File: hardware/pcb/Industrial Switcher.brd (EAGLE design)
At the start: 100 x 100 mm, 45 parts, among them IC1 MSP430FR5739, IC2 HY-TFT220, Q1 IRFR5305, Q2 32 kHz, Q3 IRFZ34NS, Q4 IRFZ34NS, Q5 IRFZ34NS, Q6 IRFZ34NS, U1 TDA3664, U2 TPS76933, U3 LT1161CSWPBF

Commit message: Routing almost finished.
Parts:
- added C14: 68uF, rcl:PANASONIC_F
- added H1, H2, H3, H4: (no value), holes:3,0
- added POWER: (no value), SparkFun:SCREWTERMINAL-5MM-2
- C13: device rcl:C0603 -> rcl:C0805
- C6: value 100uF -> 68uF; device rcl:PANASONIC_G -> rcl:PANASONIC_F
- moved C13 255.4 mm to (15.7, 4.32), flipped to the bottom, turned to 180 degrees
- moved JP1 237.5 mm to (29.5, 3.30)
- moved IC2 234.8 mm to (13.0, 1.78), turned to 270 degrees
- moved LOAD1 221.3 mm to (84.8, 41.1), turned to 90 degrees
- moved Q2 220.2 mm to (20.6, 23.4)
- moved C3 217.6 mm to (23.1, 23.4), turned to 90 degrees
- moved C2 211.6 mm to (18.0, 23.4), turned to 90 degrees
- moved C6 204.2 mm to (40.6, 36.8), flipped to the bottom, turned to 270 degrees
- moved Q3 197.7 mm to (71.9, 38.1), flipped to the bottom
- moved LOAD2 188.7 mm to (84.8, 28.7), turned to 90 degrees
- moved R8 183.8 mm to (42.4, 28.1), flipped to the bottom, turned to 180 degrees
- moved Q4 166.3 mm to (56.9, 38.1), flipped to the bottom
- moved LOAD3 159.6 mm to (84.8, 16.3), turned to 90 degrees
- moved R9 156.0 mm to (42.4, 25.5), flipped to the bottom, turned to 180 degrees
- moved LOAD4 133.8 mm to (84.8, 3.81), turned to 90 degrees
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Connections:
- removed net N$1: D1.C, Q1.3, U1.1
- removed net N$16: R9.1, U3.17
- removed net N$17: R8.1, U3.19
- new net N$23: Q5.1, U3.16
- new net N$24: Q4.1, U3.14
- new net N$25: Q3.1, U3.12
- net +24V: now also C14.+, D1.C, Q1.3, U1.1; no longer Q1.4
- net GND: now also C14.-, POWER.2
- net N$10: now also R11.1, U3.19; no longer Q4.1, U3.16
- net N$13: now also POWER.1, Q1.4; no longer Q3.1, U3.18
- net N$18: now also Q6.1, U3.18; no longer R10.1, U3.15
- net N$4: now also R8.1; no longer R11.1
- net N$5: now also R9.1, U3.15; no longer Q6.1, U3.12
- net N$7: now also R10.1, U3.17; no longer Q5.1, U3.14
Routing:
- net +24V: track 0.00 -> 287.7 mm, vias 0 -> 6
- net N$25: track 0.00 -> 39.9 mm
- net N$18: track 0.00 -> 37.0 mm
- net N$13: track 0.00 -> 29.7 mm
- net N$24: track 0.00 -> 23.5 mm
- net N$23: track 0.00 -> 18.5 mm
- net +5V: track 0.00 -> 13.0 mm
- net N$2: track 0.00 -> 3.21 mm
- net N$7: track 0.00 -> 2.37 mm
- net N$5: track 0.00 -> 2.37 mm
- net N$4: track 0.00 -> 2.37 mm
- net N$10: track 0.00 -> 2.37 mm
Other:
- board size 100 x 100 mm -> 90 x 50 mm

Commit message: Rearranged pins for better layout.
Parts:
- moved H1 320.0 mm to (78.2, 43.8)
- moved H2 293.9 mm to (79.0, 6.48)
- moved C12 250.0 mm to (27.9, 20.8), turned to 90 degrees
- moved C10 235.7 mm to (25.1, 20.1), flipped to the bottom, turned to 180 degrees
- moved R12 234.8 mm to (25.4, 10.7)
- moved C9 232.9 mm to (25.7, 21.8), flipped to the bottom, turned to 180 degrees
- moved C11 230.3 mm to (25.4, 9.53)
- moved C8 224.9 mm to (19.3, 20.1), flipped to the bottom, turned to 180 degrees
- moved C7 222.0 mm to (19.3, 21.8), flipped to the bottom, turned to 180 degrees
- moved R2 207.9 mm to (31.0, 20.4)
- moved R3 205.8 mm to (31.0, 23.0)
- moved R4 203.6 mm to (31.0, 25.5)
- moved R5 201.4 mm to (31.0, 28.1)
- moved JP1 3.59 mm to (26.2, 1.91)
- moved R10 2.79 mm to (45.2, 23.0)
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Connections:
- net CS: now also IC1.2; no longer IC1.17
- net DB0: now also IC1.12; no longer IC1.9
- net DB1: now also IC1.11; no longer IC1.10
- net DB2: now also IC1.8; no longer IC1.11
- net DB3: now also IC1.7; no longer IC1.12
- net DB4: now also IC1.6; no longer IC1.13
- net DB5: now also IC1.5; no longer IC1.14
- net DB6: now also IC1.4; no longer IC1.15
- net DB7: now also IC1.3; no longer IC1.16
- net DCLK: now also IC1.27; no longer IC1.29
- net DCS: now also IC1.26; no longer IC1.28
- net DIN: now also IC1.25; no longer IC1.27
- net DIRQ: now also IC1.23; no longer IC1.25
- net DOUT: now also IC1.24; no longer IC1.26
- net LCDRESET: now also IC1.1; no longer IC1.18
- net NTC1: now also IC1.9; no longer IC1.5
- net NTC2: now also IC1.10; no longer IC1.6
- net OUT1: now also IC1.28; no longer IC1.1
- net OUT2: now also IC1.29; no longer IC1.2
- net OUT3: now also IC1.34; no longer IC1.3
- net OUT4: now also IC1.35; no longer IC1.4
- net RS: now also IC1.14; no longer IC1.7
- net WR: now also IC1.13; no longer IC1.8
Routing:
- net LCDRESET: track 0.00 -> 25.7 mm
- net TX: track 0.00 -> 25.7 mm, vias 0 -> 1
- net CS: track 0.00 -> 21.3 mm
- net DB7: track 0.00 -> 19.4 mm
- net RX: track 0.00 -> 17.7 mm
- net DB6: track 0.00 -> 17.5 mm
- net DB5: track 0.00 -> 15.7 mm
- net OUT4: track 0.00 -> 15.5 mm, vias 0 -> 1
- net SBWTDIO: track 0.00 -> 14.0 mm
- net DB4: track 0.00 -> 13.8 mm
- net SBWTCK: track 0.00 -> 13.7 mm
- net OUT3: track 0.00 -> 13.6 mm, vias 0 -> 1
- net OUT2: track 0.00 -> 11.9 mm, vias 0 -> 1
- net DB3: track 0.00 -> 11.9 mm
- net RS: track 0.00 -> 11.5 mm
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
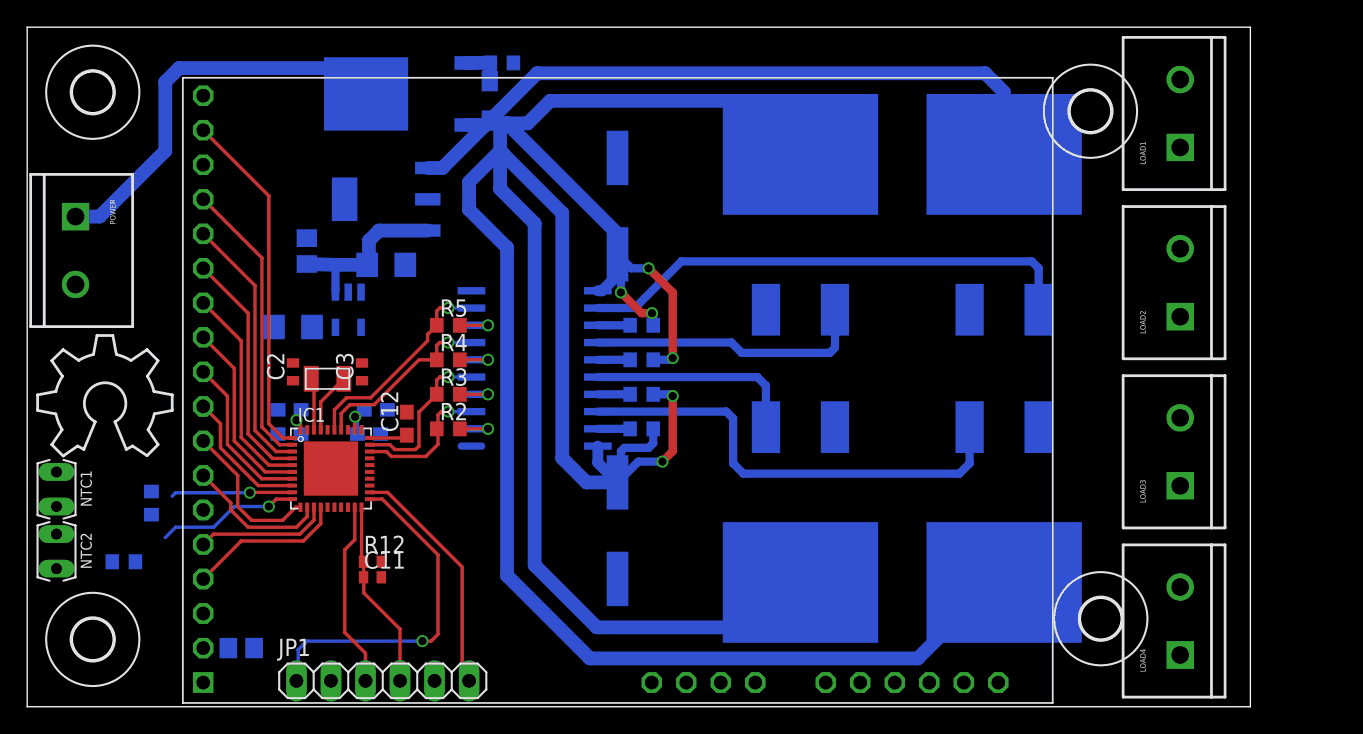
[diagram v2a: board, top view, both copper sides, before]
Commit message: Added LEDs and did some more routing.
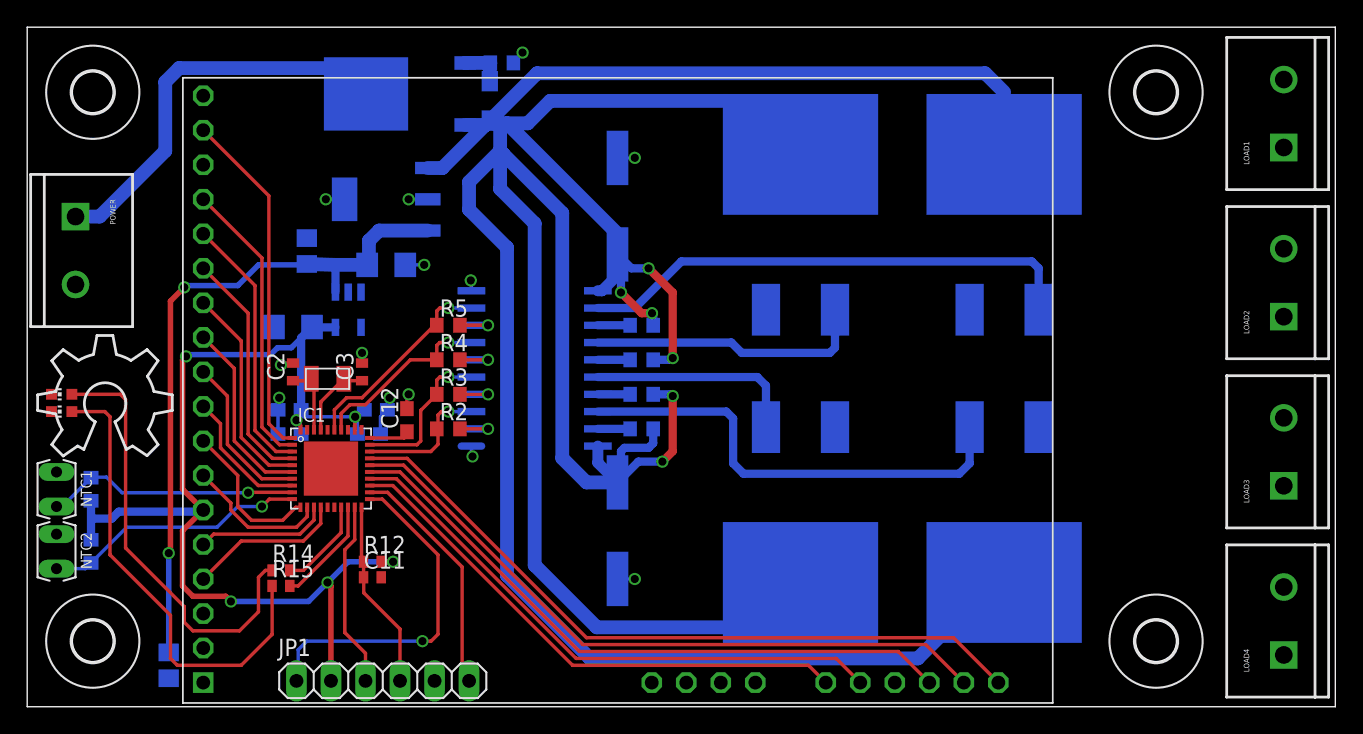
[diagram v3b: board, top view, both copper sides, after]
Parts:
- added LED1, LED2: (no value), led:CHIP-LED0603
- added R14, R15: 1k, rcl:R0402
- moved LOAD1 7.62 mm to (92.5, 41.1)
- moved LOAD2 7.62 mm to (92.5, 28.7)
- moved LOAD3 7.62 mm to (92.5, 16.3)
- moved LOAD4 7.62 mm to (92.5, 3.81)
- moved C13 5.48 mm to (10.4, 3.05), turned to 90 degrees
- moved H1 5.02 mm to (83.1, 45.2)
- moved R6 4.56 mm to (4.70, 16.0), turned to 270 degrees
- moved H2 4.39 mm to (83.1, 4.83)
- moved R7 2.53 mm to (4.70, 11.4), turned to 90 degrees
- moved C12 0.25 mm to (27.9, 21.1)
- moved H3 0.13 mm to (4.83, 4.83)
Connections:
- new net LED1: IC1.17, R14.2
- new net LED2: IC1.18, R15.2
- new net N$26: LED1.A, R14.1
- new net N$27: LED2.A, R15.1
- net GND: now also LED1.C, LED2.C
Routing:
- net +3V3: track 6.08 -> 82.7 mm, vias 2 -> 6
- net DCLK: track 0.00 -> 53.1 mm
- net DCS: track 0.00 -> 50.3 mm
- net DIN: track 0.00 -> 47.6 mm
- net DOUT: track 0.00 -> 42.3 mm
- net DIRQ: track 0.00 -> 39.6 mm
- net +5V: track 13.0 -> 50.0 mm, vias 0 -> 2
- net N$27: track 0.00 -> 34.8 mm
- net N$26: track 0.00 -> 32.3 mm
- net GND: track 0.00 -> 18.0 mm, vias 0 -> 13
- net NTC1: track 8.95 -> 18.7 mm
- net NTC2: track 10.5 -> 19.5 mm
- net LED2: track 0.00 -> 7.92 mm
- net LED1: track 0.00 -> 6.80 mm
- net N$19: track 4.46 -> 5.86 mm
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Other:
- board size 90 x 50 mm -> 96.2 x 50 mm

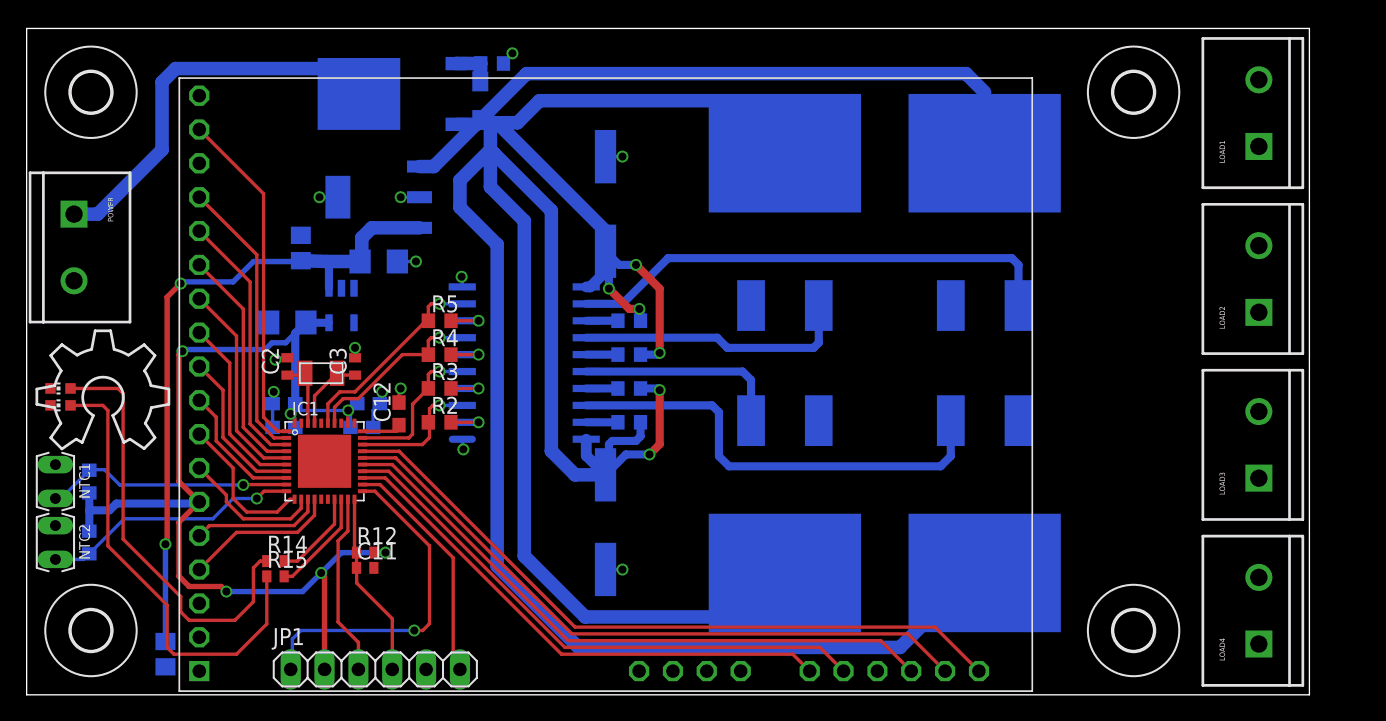
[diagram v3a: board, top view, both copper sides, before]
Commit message: PCB seems to be now ready
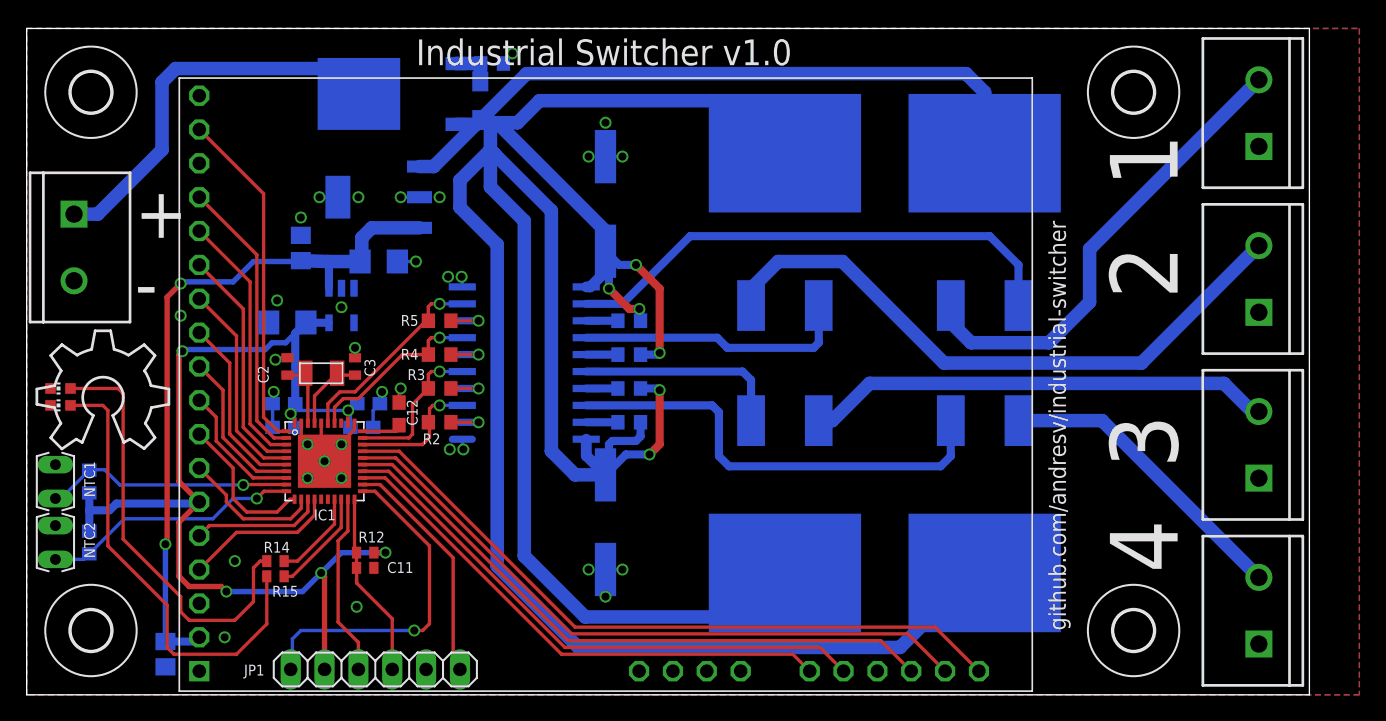
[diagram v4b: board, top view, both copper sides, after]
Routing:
- net N$12: track 0.00 -> 47.0 mm
- net N$15: track 0.00 -> 35.5 mm
- net N$9: track 0.00 -> 35.1 mm
- net N$6: track 0.00 -> 22.9 mm
- net +24V: track 284.2 -> 290.9 mm
- net GND: track 18.0 -> 24.8 mm, vias 13 -> 33
- net +5V: track 50.0 -> 52.7 mm
- net N$25: track 37.1 -> 38.5 mm
- added copper zone on layer 1, net GND
- added copper zone on layer 16, net GND
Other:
- board text added: "+"
- board text added: "-"
- board text added: "1"
- board text added: "2"
- board text added: "3"
- board text added: "4"
- board text added: "Industrial Switcher v1.0"
- board text added: "github.com/andresv/industrial-switcher"

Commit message: Added optional flyback diodes to loads.
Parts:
- added D2, D3, D4, D5: 1N4148WS, diode:SOD323-W
- moved R15 6.77 mm to (15.2, 3.05)
- moved R14 5.61 mm to (15.2, 5.59)
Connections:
- net GND: now also D2.A, D3.A, D4.A, D5.A
- net N$12: now also D4.C
- net N$15: now also D5.C
- net N$6: now also D3.C
- net N$9: now also D2.C
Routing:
- net GND: track 24.8 -> 35.8 mm, vias 33 -> 42
- net N$27: track 34.8 -> 26.7 mm
- net LED2: track 7.92 -> 15.7 mm
- net LED1: track 6.80 -> 13.7 mm
- net N$26: track 32.3 -> 25.6 mm
- net N$9: track 35.1 -> 37.8 mm
- net N$6: track 22.9 -> 25.6 mm
- net N$15: track 35.5 -> 36.3 mm

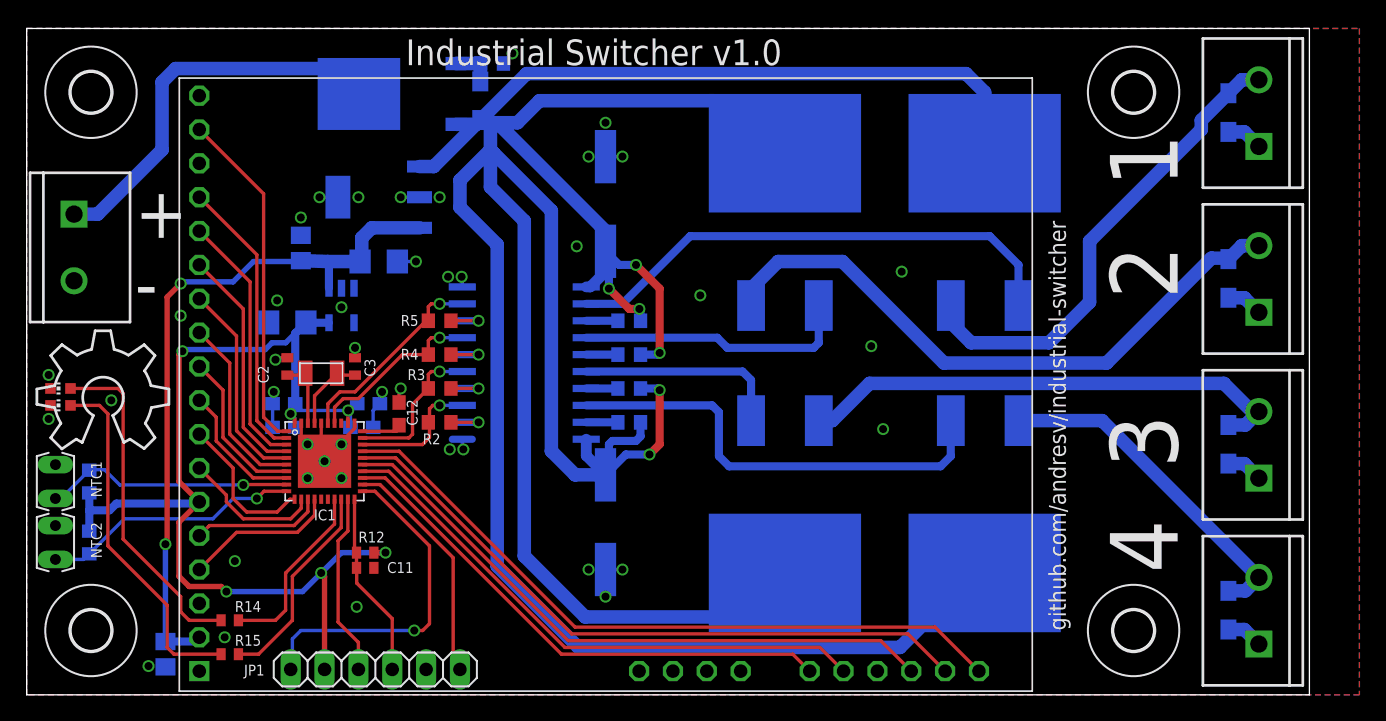
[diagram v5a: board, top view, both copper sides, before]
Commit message: Separated digital and power groundplane.
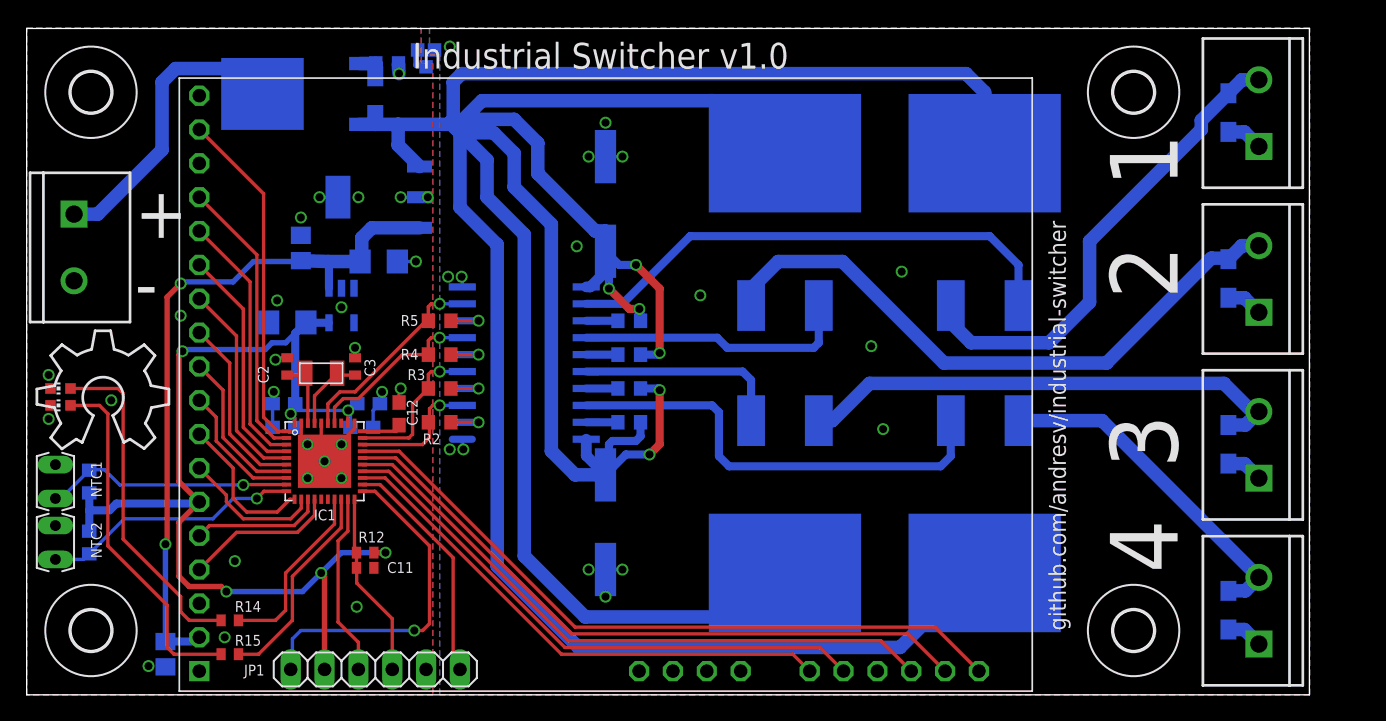
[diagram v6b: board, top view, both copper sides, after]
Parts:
- added U$1: GND_CONNECT, SparkFun-Passives:GND_CONNECT
- moved D1 7.88 mm to (26.2, 45.0)
- moved R1 7.87 mm to (27.1, 47.4)
- moved Q1 7.24 mm to (20.2, 45.1)
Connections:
- new net GNDA: C14.-, C6.-, D2.A, D3.A, D4.A, D5.A, LOAD1.1, LOAD2.1, LOAD3.1, LOAD4.1, U$1.2, U3.1, U3.10
- net GND: now also U$1.1, U$1.3; no longer C14.-, C6.-, D2.A, D3.A, D4.A, D5.A, LOAD1.1, LOAD2.1, LOAD3.1, LOAD4.1, U3.1, U3.10
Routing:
- net +24V: track 290.9 -> 310.8 mm
- net GNDA: track 0.00 -> 15.3 mm, vias 0 -> 16
- net GND: track 35.8 -> 22.4 mm, vias 42 -> 27
- net N$13: track 29.7 -> 24.8 mm
- net N$2: track 3.21 -> 2.19 mm
- added copper zone on layer 1, net GNDA
- added copper zone on layer 16, net GNDA
